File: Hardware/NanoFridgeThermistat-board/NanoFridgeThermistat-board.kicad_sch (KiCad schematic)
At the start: 36 parts, among them J1 Connector_Thermistor, J2 Main_Connector, J3 CompressorMotor_Connector, J4 I2C_Conn, SW1 SW_Push, SW2 SW_Push, T1 CST1, U1 MOC3042M, U2 TL072

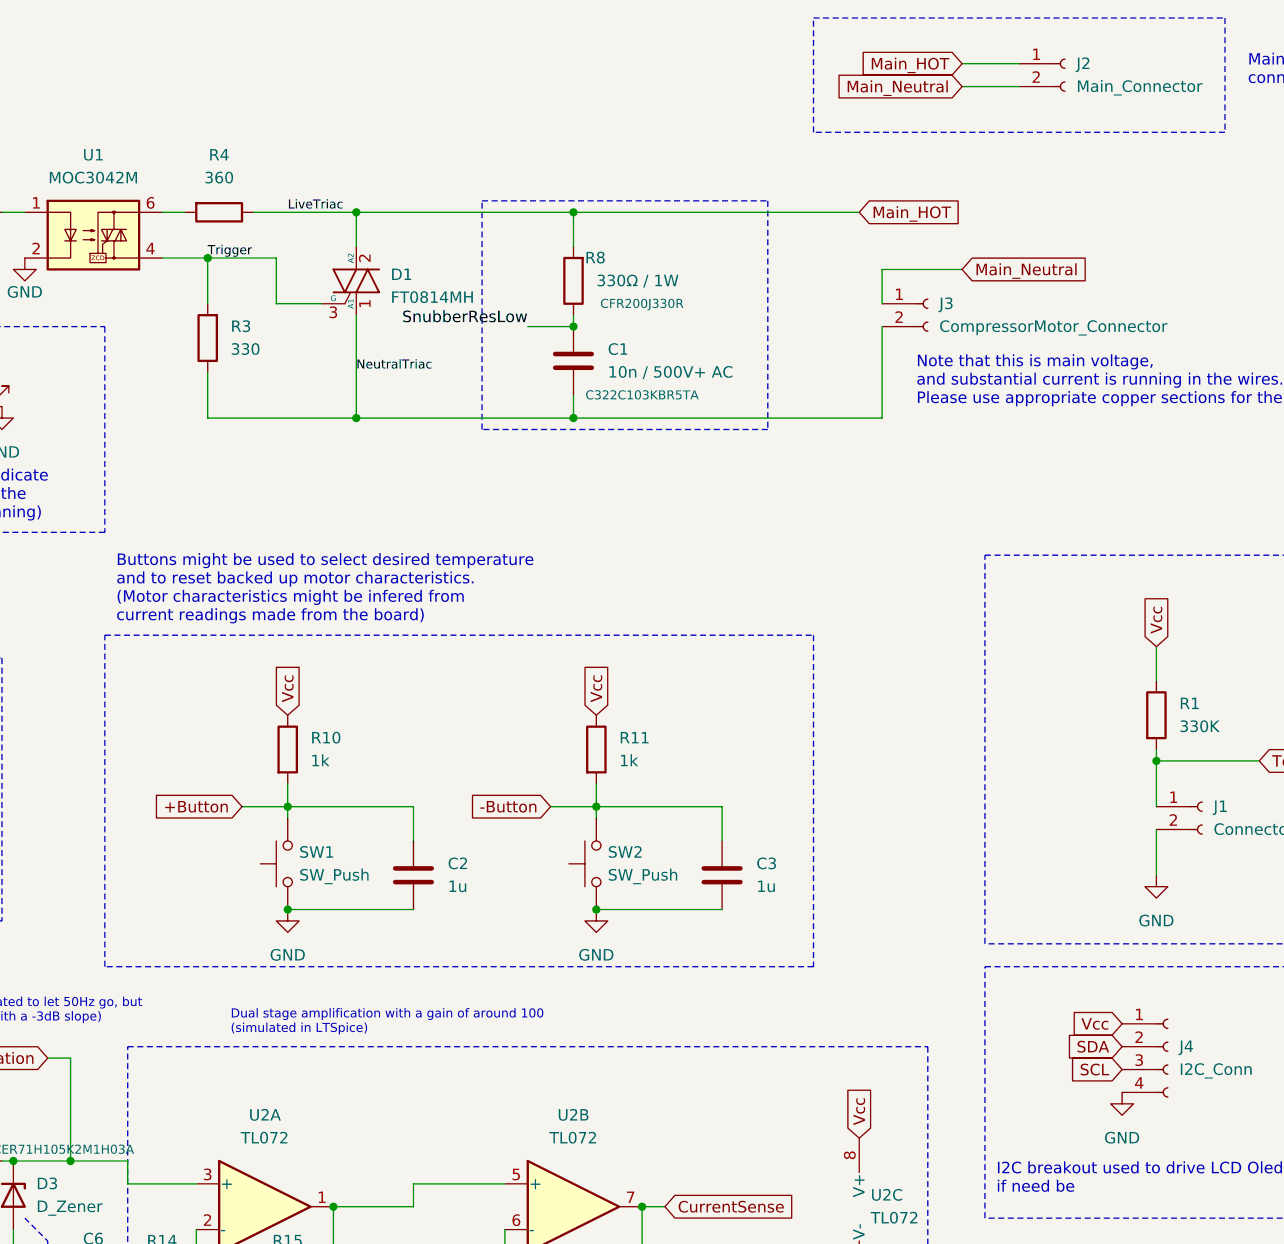
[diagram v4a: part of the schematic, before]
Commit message: Upgraded board with new models, components and layout
Signed-off-by: bebenlebricolo <benoittarrade@hotmail.fr>
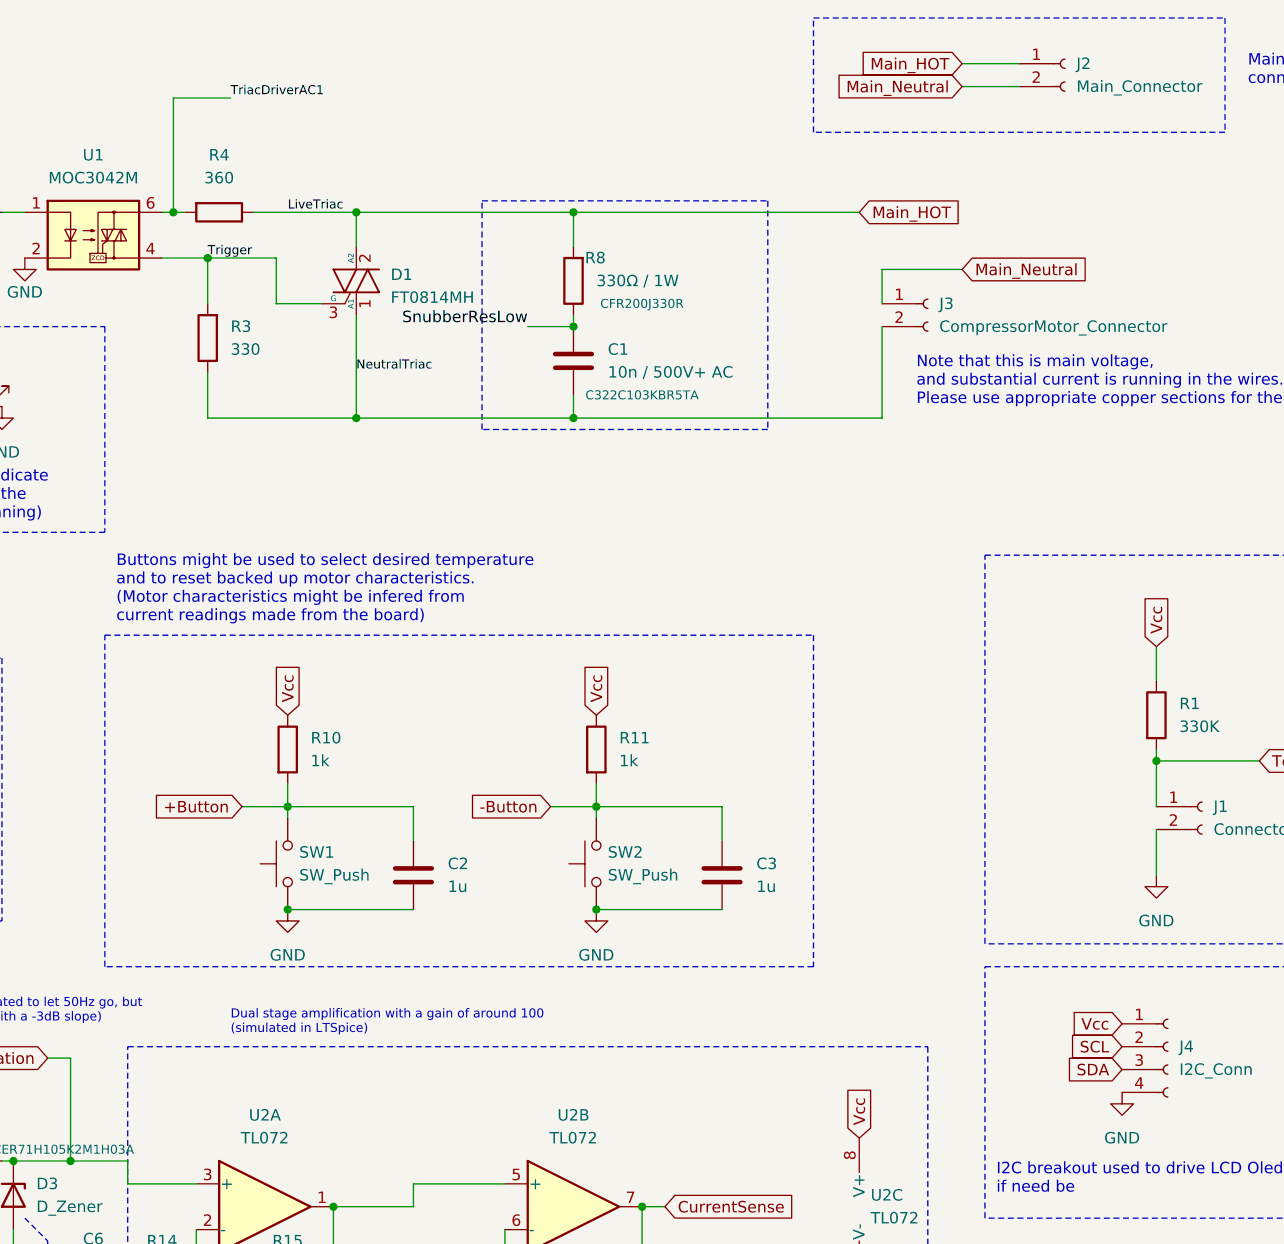
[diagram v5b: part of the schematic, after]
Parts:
- J2, J3: footprint TerminalBlock:TerminalBlock_bornier-2_P5.08mm -> TEConnectors:TE-282836-2-5.08mm
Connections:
- net SCL: now also J4.2 (Pin_2); no longer J4.3 (Pin_3)
- net SDA: now also J4.3 (Pin_3); no longer J4.2 (Pin_2)
- net TriacDriverAC1: now reaches R4.2, U1.6
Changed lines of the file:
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@@
   (junction (at 125.73 140.97) (diameter 0) (color 0 0 0 0)
+  )
+  (junction (at 137.16 35.56) (diameter 0) (color 0 0 0 0)
   )
   (junction (at 107.95 140.97) (diameter 0) (color 0 0 0 0)
@@
     (stroke (width 0) (type default))
   )
+  (wire (pts (xy 137.16 35.56) (xy 137.16 22.86))
+    (stroke (width 0) (type default))
+  )
+  (wire (pts (xy 137.16 22.86) (xy 143.51 22.86))
+    (stroke (width 0) (type default))
+  )
   (wire (pts (xy 153.67 45.72) (xy 148.59 45.72))
     (stroke (width 0) (type default))
@@
     (stroke (width 0) (type dash_dot_dot))
   )
-  (wire (pts (xy 135.89 35.56) (xy 138.43 35.56))
+  (wire (pts (xy 135.89 35.56) (xy 137.16 35.56))
     (stroke (width 0) (type default))
   )
@@
   )
   (wire (pts (xy 148.59 40.64) (xy 140.97 40.64))
+    (stroke (width 0) (type default))
+  )
+  (wire (pts (xy 137.16 35.56) (xy 138.43 35.56))
     (stroke (width 0) (type default))
   )
@@
   (label "SnubberResLow" (at 176.53 48.26 180) (fields_autoplaced)
     (effects (font (size 1.27 1.27)) (justify right bottom))
+  )
+  (label "TriacDriverAC1" (at 143.51 22.86 0) (fields_autoplaced)
+    (effects (font (size 1 1)) (justify left bottom))
   )
   (label "NeutralTriac" (at 157.48 53.34 0) (fields_autoplaced)
@@
     )
   )
-  (global_label "SDA" (shape input) (at 242.57 128.27 180) (fields_autoplaced)
+  (global_label "SDA" (shape input) (at 242.57 130.81 180) (fields_autoplaced)
     (effects (font (size 1.27 1.27)) (justify right))
-    (property "Intersheetrefs" "${INTERSHEET_REFS}" (at 236.0167 128.27 0)
+    (property "Intersheetrefs" "${INTERSHEET_REFS}" (at 236.0167 130.81 0)
       (effects (font (size 1.27 1.27)) (justify right) hide)
     )
@@
     )
   )
-  (global_label "SCL" (shape input) (at 242.57 130.81 180) (fields_autoplaced)
+  (global_label "SCL" (shape input) (at 242.57 128.27 180) (fields_autoplaced)
     (effects (font (size 1.27 1.27)) (justify right))
-    (property "Intersheetrefs" "${INTERSHEET_REFS}" (at 236.0772 130.81 0)
+    (property "Intersheetrefs" "${INTERSHEET_REFS}" (at 236.0772 128.27 0)
       (effects (font (size 1.27 1.27)) (justify right) hide)
     )
@@
       (effects (font (size 1.27 1.27)) (justify left))
     )
-    (property "Footprint" "TerminalBlock:TerminalBlock_bornier-2_P5.08mm" (at 220.98 45.72 0)
+    (property "Footprint" "TEConnectors:TE-282836-2-5.08mm" (at 220.98 45.72 0)
       (effects (font (size 1.27 1.27)) hide)
     )
@@
       (effects (font (size 1.27 1.27)) (justify left))
     )
-    (property "Footprint" "TerminalBlock:TerminalBlock_bornier-2_P5.08mm" (at 236.22 19.05 0)
-      (effects (font (size 1.27 1.27)) hide)
-    )
+    (property "Footprint" "TEConnectors:TE-282836-2-5.08mm" (at 236.22 19.05 0)
+      (effects (font (size 1.27 1.27)) hide)
+    )

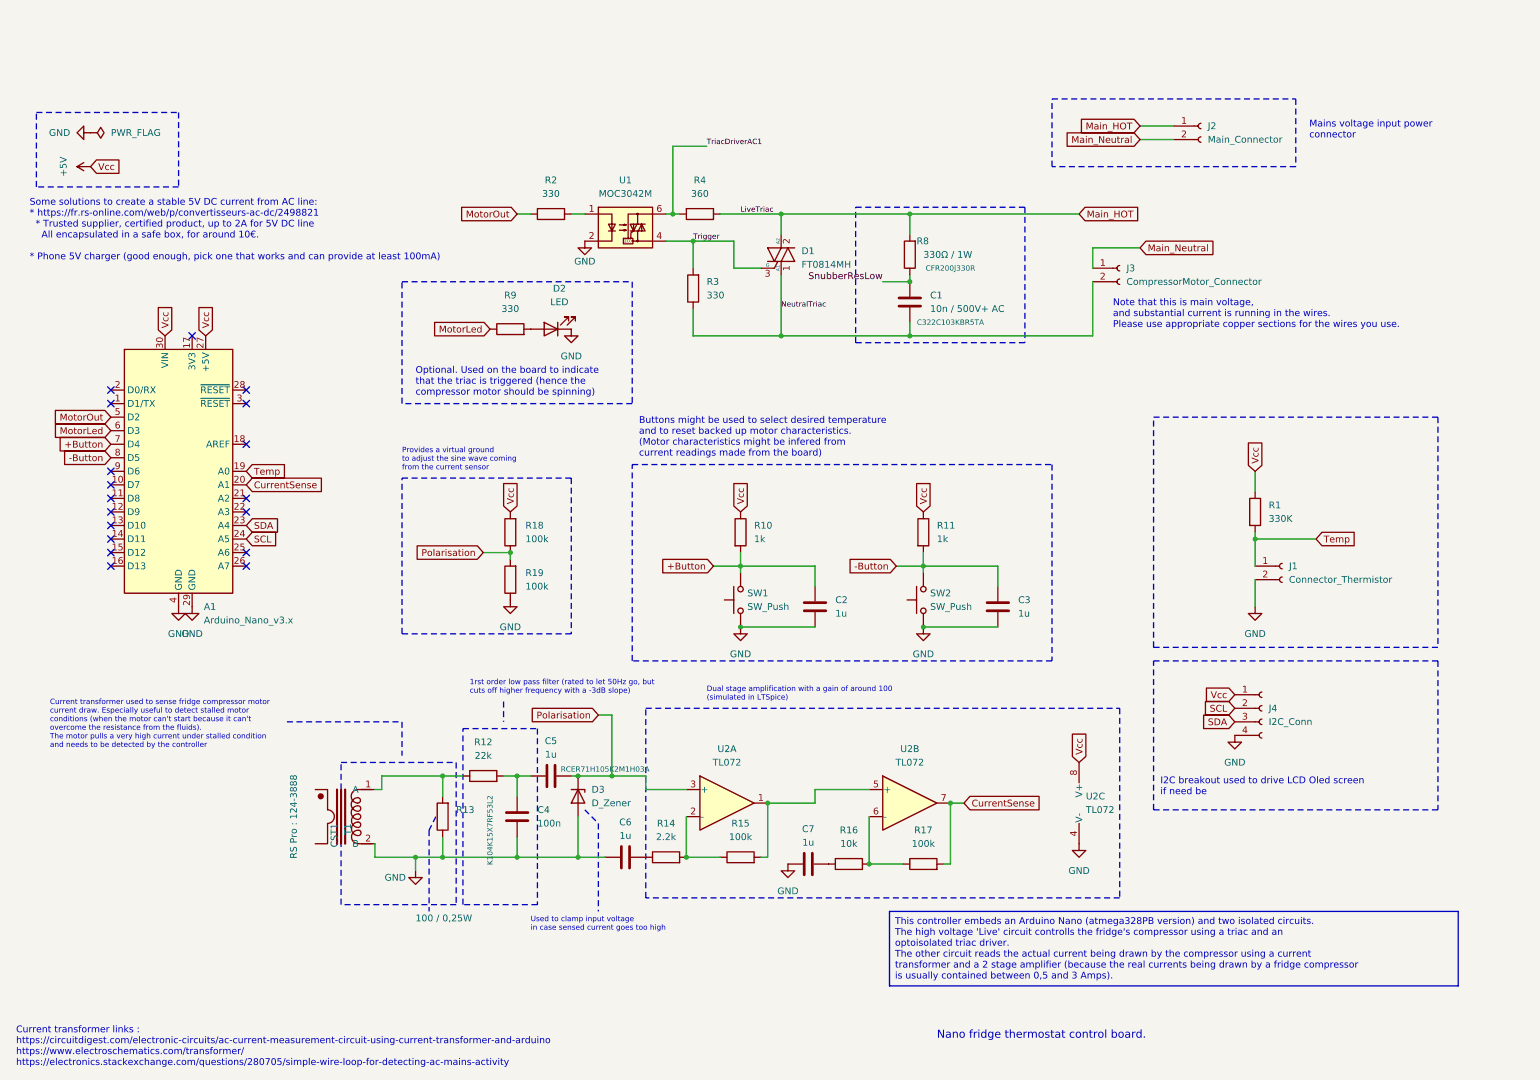
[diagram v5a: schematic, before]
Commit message: Adding mounting holes and test points
Signed-off-by: bebenlebricolo <benoittarrade@hotmail.fr>
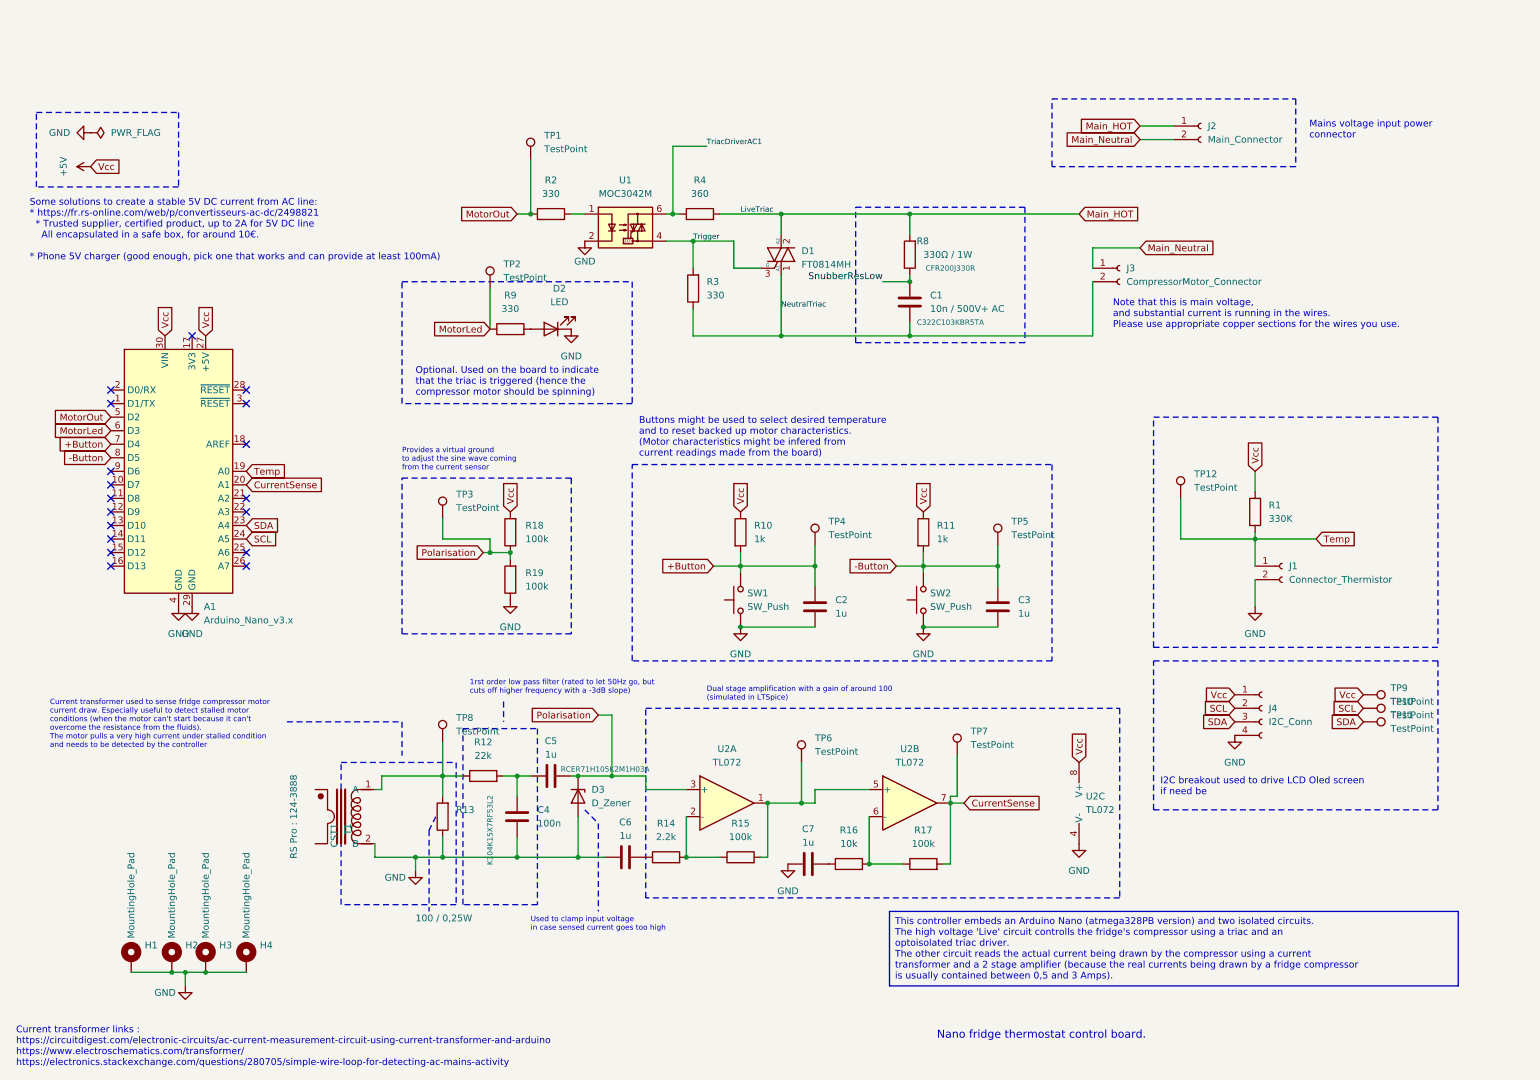
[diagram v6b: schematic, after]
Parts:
- added H1, H2, H3, H4: MountingHole_Pad, MountingHole:MountingHole_2.2mm_M2_DIN965_Pad, symbol Mechanical:MountingHole_Pad
- added TP1, TP10, TP11, TP12, TP2, TP3, TP4, TP5, TP6, TP7, TP8, TP9: TestPoint, TestPoint:TestPoint_Pad_D2.0mm, symbol Connector:TestPoint
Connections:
- net +5V: now also TP9.1
- net +Button: now also TP4.1
- net -Button: now also TP5.1
- net CurrentSense: now also TP7.1
- net GND: now also H1.1, H2.1, H3.1, H4.1
- net MotorLed: now also TP2.1
- net MotorOut: now also TP1.1
- net Polarisation: now also TP3.1
- net SCL: now also TP10.1
- net SDA: now also TP11.1
- net Temp: now also TP12.1
- net at R15.2, U2.1, U2.5 (+): now also TP6.1
- net at R12.1, R13.2, T1.1 (A): now also TP8.1

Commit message: Finalized board with testing points and mouse bites to detach AC board
Signed-off-by: bebenlebricolo <benoittarrade@hotmail.fr>
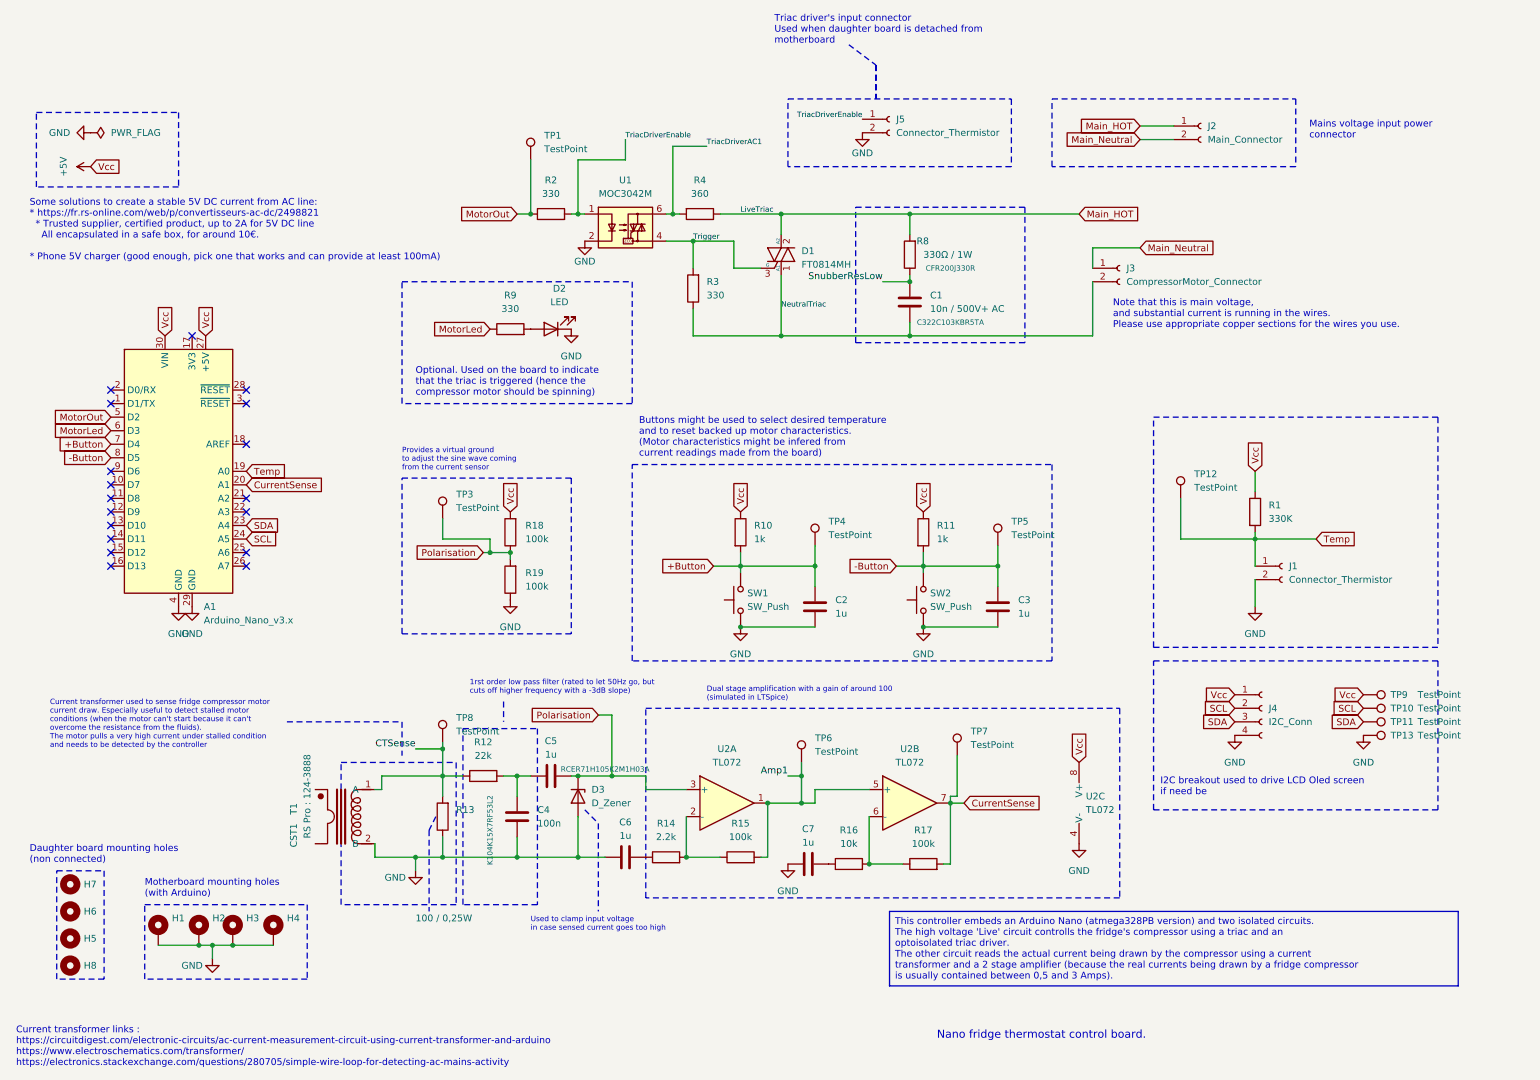
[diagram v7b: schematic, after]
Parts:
- removed TP2: TestPoint, TestPoint:TestPoint_Pad_D2.0mm, symbol Connector:TestPoint
- added H5, H6, H7, H8: MountingHole, MountingHole:MountingHole_2.2mm_M2_ISO7380, symbol Mechanical:MountingHole
- added J5: Connector_Thermistor, Connector_PinSocket_2.54mm:PinSocket_1x02_P2.54mm_Vertical, symbol Connector:Conn_01x02_Socket
- added TP13: TestPoint, TestPoint:TestPoint_Pad_D1.0mm, symbol Connector:TestPoint
- TP1, TP10, TP11, TP12, TP3, TP4, TP5, TP6, TP7, TP8, TP9: footprint TestPoint:TestPoint_Pad_D2.0mm -> TestPoint:TestPoint_Pad_D1.0mm
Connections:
- net GND: now also J5.2 (Pin_2), TP13.1
- net TriacDriverEnable: now reaches R2.2, U1.1
- net TriacDriverEnable: now also J5.1 (Pin_1)
- net Amp1: now reaches R15.2, TP6.1, U2.1, U2.5 (+)
- net CTSense: now reaches R12.1, R13.2, T1.1 (A), TP8.1
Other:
- note added: "Daughter board mounting holes (non connected)"
- note added: "Motherboard mounting holes (with Arduino)"
- note added: "Triac driver's input connector Used when daughter board is detached from motherboard"
- moved on the sheet: H1, H2, H3, H4
